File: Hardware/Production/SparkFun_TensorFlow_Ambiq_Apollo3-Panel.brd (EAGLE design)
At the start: 175.6 x 134.7 mm, 906 parts, among them J12 CORTEX_DEBUG, J14 CAMERA-OV7670, J18 CORTEX_DEBUG, J20 CAMERA-OV7670, J24 CORTEX_DEBUG, J26 CAMERA-OV7670, J30 CORTEX_DEBUG, J32 CAMERA-OV7670, J36 CORTEX_DEBUG, J38 CAMERA-OV7670, J42 CORTEX_DEBUG, J44 CAMERA-OV7670, J48 CORTEX_DEBUG, J5 CORTEX_DEBUG, J50 CAMERA-OV7670, J54 CORTEX_DEBUG, J6 CAMERA-OV7670, J8 CAMERA-OV7670, U1 LIS2DH12, U10 LIS2DH12, U11 1.8V, U12 ARTEMIS_MODULESMD, U13 LIS2DH12, U14 1.8V, U15 ARTEMIS_MODULESMD, U16 LIS2DH12, U17 1.8V, U18 ARTEMIS_MODULESMD, U19 LIS2DH12, U2 LIS2DH12, U20 1.8V, U21 ARTEMIS_MODULESMD, U22 LIS2DH12, U23 1.8V, U24 ARTEMIS_MODULESMD, U25 LIS2DH12, U26 1.8V, U27 ARTEMIS_MODULESMD, U3 1.8V, U4 1.8V, U5 ARTEMIS_MODULESMD, U6 ARTEMIS_MODULESMD, U7 LIS2DH12, U8 1.8V, U9 ARTEMIS_MODULESMD, Y1 32.768kHz, Y2 32.768kHz, Y3 32.768kHz, Y4 32.768kHz, Y5 32.768kHz, Y6 32.768kHz, Y7 32.768kHz, Y8 32.768kHz, Y9 32.768kHz

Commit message: Adding panel files for v2.1
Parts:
- removed R127, R128, R129, R130, R138, R139, R145, R146, R147, R148, R156, R157: 4.7k, SparkFun-Resistors:0603
- removed R131, R136, R137, R140, R141, R149, R154, R155, R158, R159: 10k, SparkFun-Resistors:0402-TIGHT
- removed R132, R133, R134, R135, R150, R151, R152, R153: 1k, SparkFun-Resistors:0603
- removed R142, R144, R160, R162: 100k, SparkFun-Resistors:0603
- removed R143, R161: 10k, SparkFun-Resistors:0603
- J10, J16, J22, J28, J34, J40, J46, J52: device SparkFun-Connectors:1X05_NO_SILK -> SparkFun-Connectors:JST04_1MM_RA
- J11, J17, J23, J29, J35, J41, J47, J53: value (none) -> CORTEX_DEBUG; device SparkFun-Connectors:JST04_1MM_RA -> SparkFun-Connectors:2X5-PTH-1.27MM
- J12, J18, J24, J30, J36, J42, J48, J54: value CORTEX_DEBUG -> CAMERA-HIMAX; device SparkFun-Connectors:2X5-PTH-1.27MM -> SparkFun-Connectors:FPC-24-AMPHENOL-SFV24R-1STE1HLF
- J14, J20, J26, J32, J38, J44, J50, J8: value CAMERA-OV7670 -> (none); device SparkFun-Connectors:FPC-24-AMPHENOL-SFV24R-1STE1HLF -> SparkFun-Connectors:1X05_NO_SILK
- J6: value CAMERA-OV7670 -> (none); device SparkFun-Connectors:FPC-24-AMPHENOL-SFV24R-1STE1HLF -> SparkFun-Connectors:1X06-SMD_RA_MALE
- J7: value (none) -> CAMERA-HIMAX; device SparkFun-Connectors:1X06-SMD_RA_MALE -> SparkFun-Connectors:FPC-24-AMPHENOL-SFV24R-1STE1HLF
- R10, R104, R105, R118, R119, R33, R47, R50, R64, R77, R9: value 10k -> 1k; device SparkFun-Resistors:0402-TIGHT -> SparkFun-Resistors:0603
- R100, R101, R113, R32, R46, R59, R86, R87: value 10k -> 4.7k; device SparkFun-Resistors:0402-TIGHT -> SparkFun-Resistors:0603
- R103, R120, R48, R49, R75, R76, R91, R92: value 4.7k -> 1k
- R106, R34, R36, R90: value 100k -> 1k
- R107, R53: device SparkFun-Resistors:0603 -> SparkFun-Resistors:0402-TIGHT
- R108, R52: value 100k -> 10k; device SparkFun-Resistors:0603 -> SparkFun-Resistors:0402-TIGHT
- R109, R121, R37, R38, R39, R66, R67, R93, R94: value 4.7k -> 10k; device SparkFun-Resistors:0603 -> SparkFun-Resistors:0402-TIGHT
- R110, R112, R23, R40, R56, R84: value 4.7k -> 100k
- R111, R55: value 4.7k -> 10k
- R114, R115, R116, R43, R44, R45, R60, R99: value 1k -> 4.7k
- R18, R19, R79, R80, R81: value 1k -> 10k; device SparkFun-Resistors:0603 -> SparkFun-Resistors:0402-TIGHT
- R21, R68, R82: value 10k -> 100k; device SparkFun-Resistors:0402-TIGHT -> SparkFun-Resistors:0603
- R22, R41, R69, R83: device SparkFun-Resistors:0402-TIGHT -> SparkFun-Resistors:0603
- R35, R89: value 10k -> 1k
- R42, R96, R98: value 1k -> 100k
- R71: value 10k -> 4.7k
- R72, R88: value 100k -> 4.7k
- R97: value 1k -> 10k
- S1, S2, S3, S4, S5, S6, S7, S8, S9: device SparkFun-Switches:TACTILE_SWITCH_SMD_5.2MM -> SparkFun-Switches:TACTILE_SWITCH_SMD_4.6X2.8MM
- U12, U15, U18, U21, U24, U27, U5, U6, U9: device Testing:ARTEMIS_FP -> SparkFun-IC-Microcontroller:ARTEMIS_FP
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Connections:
- removed net CAMERA_HREF: J6.9, U5.~AD13
- removed net CAMERA_HREF1: J8.9, U6.~AD13
- removed net CAMERA_HREF2: J14.9, U9.~AD13
- removed net CAMERA_HREF3: J20.9, U12.~AD13
- removed net CAMERA_HREF4: J26.9, U15.~AD13
- removed net CAMERA_HREF5: J32.9, U18.~AD13
- removed net CAMERA_HREF6: J38.9, U21.~AD13
- removed net CAMERA_HREF7: J44.9, U24.~AD13
- removed net CAMERA_HREF8: J50.9, U27.~AD13
- removed net CAMERA_PWDN: J6.8, R22.2, U5.D15
- removed net CAMERA_PWDN1: J8.8, R21.2, U6.D15
- removed net CAMERA_PWDN2: J14.8, R47.2, U9.D15
- removed net CAMERA_PWDN3: J20.8, R65.2, U12.D15
- removed net CAMERA_PWDN4: J26.8, R83.2, U15.D15
- removed net CAMERA_PWDN5: J32.8, R101.2, U18.D15
- removed net CAMERA_PWDN6: J38.8, R119.2, U21.D15
- removed net CAMERA_PWDN7: J44.8, R137.2, U24.D15
- removed net CAMERA_PWDN8: J50.8, R155.2, U27.D15
- removed net CAMERA_RESET: J6.6, R10.1, U5.~AD11
- removed net CAMERA_RESET1: J8.6, R9.1, U6.~AD11
- removed net CAMERA_RESET2: J14.6, R41.1, U9.~AD11
- removed net CAMERA_RESET3: J20.6, R59.1, U12.~AD11
- removed net CAMERA_RESET4: J26.6, R77.1, U15.~AD11
- removed net CAMERA_RESET5: J32.6, R95.1, U18.~AD11
- removed net CAMERA_RESET6: J38.6, R113.1, U21.~AD11
- removed net CAMERA_RESET7: J44.6, R131.1, U24.~AD11
- removed net CAMERA_RESET8: J50.6, R149.1, U27.~AD11
- removed net CAMERA_XCLK: J6.13, U5.~AD32
- removed net CAMERA_XCLK1: J8.13, U6.~AD32
- removed net CAMERA_XCLK2: J14.13, U9.~AD32
- removed net CAMERA_XCLK3: J20.13, U12.~AD32
- removed net CAMERA_XCLK4: J26.13, U15.~AD32
- removed net CAMERA_XCLK5: J32.13, U18.~AD32
- removed net CAMERA_XCLK6: J38.13, U21.~AD32
- removed net CAMERA_XCLK7: J44.13, U24.~AD32
- removed net CAMERA_XCLK8: J50.13, U27.~AD32
- removed net CAMERA_Y0: J6.19, U5.~D22
- removed net CAMERA_Y1: J6.21, U5.~D4
- removed net CAMERA_Y10: J8.22, U6.~AD35
- removed net CAMERA_Y11: J8.18, U6.~D23
- removed net CAMERA_Y12: J8.19, U6.~D22
- removed net CAMERA_Y13: J8.12, U6.~D26
- removed net CAMERA_Y14: J8.14, U6.~D6
- removed net CAMERA_Y15: J8.16, U6.~D28
- removed net CAMERA_Y16: J14.20, U9.~D24
- removed net CAMERA_Y17: J14.21, U9.~D4
- removed net CAMERA_Y18: J14.22, U9.~AD35
- removed net CAMERA_Y19: J14.18, U9.~D23
- removed net CAMERA_Y2: J6.22, U5.~AD35
- removed net CAMERA_Y20: J14.19, U9.~D22
- removed net CAMERA_Y21: J14.12, U9.~D26
- removed net CAMERA_Y22: J14.14, U9.~D6
- removed net CAMERA_Y23: J14.16, U9.~D28
- removed net CAMERA_Y24: J20.20, U12.~D24
- removed net CAMERA_Y25: J20.21, U12.~D4
- removed net CAMERA_Y26: J20.22, U12.~AD35
- removed net CAMERA_Y27: J20.18, U12.~D23
- removed net CAMERA_Y28: J20.19, U12.~D22
- removed net CAMERA_Y29: J20.12, U12.~D26
- removed net CAMERA_Y3: J6.20, U5.~D24
- removed net CAMERA_Y30: J20.14, U12.~D6
- removed net CAMERA_Y31: J20.16, U12.~D28
- removed net CAMERA_Y32: J26.20, U15.~D24
- removed net CAMERA_Y33: J26.21, U15.~D4
- removed net CAMERA_Y34: J26.22, U15.~AD35
- removed net CAMERA_Y35: J26.18, U15.~D23
- removed net CAMERA_Y36: J26.19, U15.~D22
- removed net CAMERA_Y37: J26.12, U15.~D26
- removed net CAMERA_Y38: J26.14, U15.~D6
- removed net CAMERA_Y39: J26.16, U15.~D28
- removed net CAMERA_Y4: J6.18, U5.~D23
- removed net CAMERA_Y40: J32.20, U18.~D24
- removed net CAMERA_Y41: J32.21, U18.~D4
- removed net CAMERA_Y42: J32.22, U18.~AD35
- removed net CAMERA_Y43: J32.18, U18.~D23
- removed net CAMERA_Y44: J32.19, U18.~D22
- removed net CAMERA_Y45: J32.12, U18.~D26
- removed net CAMERA_Y46: J32.14, U18.~D6
- removed net CAMERA_Y47: J32.16, U18.~D28
- removed net CAMERA_Y48: J38.20, U21.~D24
- removed net CAMERA_Y49: J38.21, U21.~D4
- removed net CAMERA_Y5: J6.16, U5.~D28
- removed net CAMERA_Y50: J38.22, U21.~AD35
- removed net CAMERA_Y51: J38.18, U21.~D23
- removed net CAMERA_Y52: J38.19, U21.~D22
- removed net CAMERA_Y53: J38.12, U21.~D26
- removed net CAMERA_Y54: J38.14, U21.~D6
- removed net CAMERA_Y55: J38.16, U21.~D28
- removed net CAMERA_Y56: J44.20, U24.~D24
- removed net CAMERA_Y57: J44.21, U24.~D4
- removed net CAMERA_Y58: J44.22, U24.~AD35
- removed net CAMERA_Y59: J44.18, U24.~D23
- removed net CAMERA_Y6: J6.14, U5.~D6
- removed net CAMERA_Y60: J44.19, U24.~D22
- removed net CAMERA_Y61: J44.12, U24.~D26
- removed net CAMERA_Y62: J44.14, U24.~D6
- removed net CAMERA_Y63: J44.16, U24.~D28
- removed net CAMERA_Y64: J50.20, U27.~D24
- removed net CAMERA_Y65: J50.21, U27.~D4
- removed net CAMERA_Y66: J50.22, U27.~AD35
- removed net CAMERA_Y67: J50.18, U27.~D23
- removed net CAMERA_Y68: J50.19, U27.~D22
- removed net CAMERA_Y69: J50.12, U27.~D26
- removed net CAMERA_Y7: J6.12, U5.~D26
- removed net CAMERA_Y70: J50.14, U27.~D6
- removed net CAMERA_Y71: J50.16, U27.~D28
- removed net CAMERA_Y8: J8.20, U6.~D24
- removed net CAMERA_Y9: J8.21, U6.~D4
- new net CAMERA_D0: J7.14, U5.D14
- new net CAMERA_D1: J7.3, U5.~AD11
- new net CAMERA_D10: J12.9, U6.~D25
- new net CAMERA_D11: J12.12, U6.~D6
- new net CAMERA_D12: J12.14, U6.D14
- new net CAMERA_D13: J12.13, U6.~D28
- new net CAMERA_D14: J12.19, U6.~AD35
- new net CAMERA_D15: J12.20, U6.~D5
- new net CAMERA_D16: J18.5, U9.AD34
- new net CAMERA_D17: J18.3, U9.~AD11
- new net CAMERA_D18: J18.9, U9.~D25
- new net CAMERA_D19: J18.12, U9.~D6
- new net CAMERA_D2: J7.9, U5.~D25
- new net CAMERA_D20: J18.14, U9.D14
- new net CAMERA_D21: J18.13, U9.~D28
- new net CAMERA_D22: J18.19, U9.~AD35
- new net CAMERA_D23: J18.20, U9.~D5
- new net CAMERA_D24: J24.5, U12.AD34
- new net CAMERA_D25: J24.3, U12.~AD11
- new net CAMERA_D26: J24.9, U12.~D25
- new net CAMERA_D27: J24.12, U12.~D6
- new net CAMERA_D28: J24.14, U12.D14
- new net CAMERA_D29: J24.13, U12.~D28
- new net CAMERA_D3: J7.5, U5.AD34
- new net CAMERA_D30: J24.19, U12.~AD35
- new net CAMERA_D31: J24.20, U12.~D5
- new net CAMERA_D32: J30.5, U15.AD34
- new net CAMERA_D33: J30.3, U15.~AD11
- new net CAMERA_D34: J30.9, U15.~D25
- new net CAMERA_D35: J30.12, U15.~D6
- new net CAMERA_D36: J30.14, U15.D14
- new net CAMERA_D37: J30.13, U15.~D28
- new net CAMERA_D38: J30.19, U15.~AD35
- new net CAMERA_D39: J30.20, U15.~D5
- new net CAMERA_D4: J7.12, U5.~D6
- new net CAMERA_D40: J36.5, U18.AD34
- new net CAMERA_D41: J36.3, U18.~AD11
- new net CAMERA_D42: J36.9, U18.~D25
- new net CAMERA_D43: J36.12, U18.~D6
- new net CAMERA_D44: J36.14, U18.D14
- new net CAMERA_D45: J36.13, U18.~D28
- new net CAMERA_D46: J36.19, U18.~AD35
- new net CAMERA_D47: J36.20, U18.~D5
- new net CAMERA_D48: J42.5, U21.AD34
- new net CAMERA_D49: J42.3, U21.~AD11
- new net CAMERA_D5: J7.20, U5.~D5
- new net CAMERA_D50: J42.9, U21.~D25
- new net CAMERA_D51: J42.12, U21.~D6
- new net CAMERA_D52: J42.14, U21.D14
- new net CAMERA_D53: J42.13, U21.~D28
- new net CAMERA_D54: J42.19, U21.~AD35
- new net CAMERA_D55: J42.20, U21.~D5
- new net CAMERA_D56: J48.5, U24.AD34
- new net CAMERA_D57: J48.3, U24.~AD11
- new net CAMERA_D58: J48.9, U24.~D25
- new net CAMERA_D59: J48.12, U24.~D6
- new net CAMERA_D6: J7.19, U5.~AD35
- new net CAMERA_D60: J48.14, U24.D14
- new net CAMERA_D61: J48.13, U24.~D28
- new net CAMERA_D62: J48.19, U24.~AD35
- new net CAMERA_D63: J48.20, U24.~D5
- new net CAMERA_D64: J54.5, U27.AD34
- new net CAMERA_D65: J54.3, U27.~AD11
- new net CAMERA_D66: J54.9, U27.~D25
- new net CAMERA_D67: J54.12, U27.~D6
- new net CAMERA_D68: J54.14, U27.D14
- new net CAMERA_D69: J54.13, U27.~D28
- new net CAMERA_D7: J7.13, U5.~D28
- new net CAMERA_D70: J54.19, U27.~AD35
- new net CAMERA_D71: J54.20, U27.~D5
- new net CAMERA_D8: J12.5, U6.AD34
- new net CAMERA_D9: J12.3, U6.~AD11
- new net CAMERA_HSYNC: J7.16, U5.~D27
- new net CAMERA_HSYNC1: J12.16, U6.~D27
- new net CAMERA_HSYNC2: J18.16, U9.~D27
- new net CAMERA_HSYNC3: J24.16, U12.~D27
- new net CAMERA_HSYNC4: J30.16, U15.~D27
- new net CAMERA_HSYNC5: J36.16, U18.~D27
- new net CAMERA_HSYNC6: J42.16, U21.~D27
- new net CAMERA_HSYNC7: J48.16, U24.~D27
- new net CAMERA_HSYNC8: J54.16, U27.~D27
- new net CAMERA_INT: J7.18, U5.~D23
- new net CAMERA_INT1: J12.18, U6.~D23
- new net CAMERA_INT2: J18.18, U9.~D23
- new net CAMERA_INT3: J24.18, U12.~D23
- new net CAMERA_INT4: J30.18, U15.~D23
- new net CAMERA_INT5: J36.18, U18.~D23
- new net CAMERA_INT6: J42.18, U21.~D23
- new net CAMERA_INT7: J48.18, U24.~D23
- new net CAMERA_INT8: J54.18, U27.~D23
- new net CAMERA_MCLK: J7.8, U5.~D26
- new net CAMERA_MCLK1: J12.8, U6.~D26
- new net CAMERA_MCLK2: J18.8, U9.~D26
- new net CAMERA_MCLK3: J24.8, U12.~D26
- new net CAMERA_MCLK4: J30.8, U15.~D26
- new net CAMERA_MCLK5: J36.8, U18.~D26
- new net CAMERA_MCLK6: J42.8, U21.~D26
- new net CAMERA_MCLK7: J48.8, U24.~D26
- new net CAMERA_MCLK8: J54.8, U27.~D26
- new net CAMERA_TRIG: J7.7, U5.~AD13
- new net CAMERA_TRIG1: J12.7, U6.~AD13
- new net CAMERA_TRIG2: J18.7, U9.~AD13
- new net CAMERA_TRIG3: J24.7, U12.~AD13
- new net CAMERA_TRIG4: J30.7, U15.~AD13
- new net CAMERA_TRIG5: J36.7, U18.~AD13
- new net CAMERA_TRIG6: J42.7, U21.~AD13
- new net CAMERA_TRIG7: J48.7, U24.~AD13
- new net CAMERA_TRIG8: J54.7, U27.~AD13
- net !DTR1: now also J6.1, R23.2; no longer J7.1, R36.2
- net !DTR2: now also R42.2; no longer R54.2
- net !DTR3: now also R56.2; no longer R72.2
- net !DTR4: now also R70.2; no longer R90.2
- net !DTR5: now also R84.2; no longer R108.2
- net !DTR6: now also R98.2; no longer R126.2
- net !DTR7: now also R112.2; no longer R144.2
- net !DTR8: now also R126.2; no longer R162.2
- net 1.8V: now also J7.10; no longer J6.10
- net 1.8V1: now also J12.10; no longer J8.10
- net 1.8V2: now also J18.10; no longer J14.10
- net 1.8V3: now also J24.10; no longer J20.10
- net 1.8V4: now also J30.10; no longer J26.10
- net 1.8V5: now also J36.10; no longer J32.10
- net 1.8V6: now also J42.10; no longer J38.10
- net 1.8V7: now also J48.10; no longer J44.10
- net 1.8V8: now also J54.10; no longer J50.10
- net A1: now also J8.2; no longer J9.2
- net A2: now also J14.2; no longer J15.2
- net A3: now also J20.2; no longer J21.2
- net A4: now also J26.2; no longer J27.2
- net A5: now also J32.2; no longer J33.2
- net A6: now also J38.2; no longer J39.2
- net A7: now also J44.2; no longer J45.2
- net A8: now also J50.2; no longer J51.2
- net ACCEL_I2C_SCL2: now also R31.1; no longer R39.1
- net ACCEL_I2C_SCL3: now also R45.1; no longer R57.1
- net ACCEL_I2C_SCL4: now also R59.1; no longer R75.1
- net ACCEL_I2C_SCL5: now also R73.1; no longer R93.1
- net ACCEL_I2C_SCL6: now also R87.1; no longer R111.1
- net ACCEL_I2C_SCL7: now also R101.1; no longer R129.1
- net ACCEL_I2C_SCL8: now also R115.1; no longer R147.1
- net ACCEL_I2C_SDA2: now also R32.1; no longer R40.1
- net ACCEL_I2C_SDA3: now also R46.1; no longer R58.1
- net ACCEL_I2C_SDA4: now also R60.1; no longer R76.1
- net ACCEL_I2C_SDA5: now also R74.1; no longer R94.1
- net ACCEL_I2C_SDA6: now also R88.1; no longer R112.1
- net ACCEL_I2C_SDA7: now also R102.1; no longer R130.1
- net ACCEL_I2C_SDA8: now also R116.1; no longer R148.1
- net ACCEL_INT10: now also R66.2; no longer R86.2
- net ACCEL_INT11: now also R81.2; no longer R105.2
- net ACCEL_INT12: now also R80.2; no longer R104.2
- net ACCEL_INT13: now also R95.2; no longer R123.2
- net ACCEL_INT14: now also R94.2; no longer R122.2
- net ACCEL_INT15: now also R109.2; no longer R141.2
- net ACCEL_INT16: now also R108.2; no longer R140.2
- net ACCEL_INT17: now also R123.2; no longer R159.2
- net ACCEL_INT18: now also R122.2; no longer R158.2
- net ACCEL_INT3: now also R20.2; no longer R33.2
- net ACCEL_INT4: now also R19.2; no longer R32.2
- net ACCEL_INT5: now also R39.2; no longer R51.2
- net ACCEL_INT6: now also R38.2; no longer R50.2
- net ACCEL_INT7: now also R53.2; no longer R69.2
- net ACCEL_INT8: now also R52.2; no longer R68.2
- net ACCEL_INT9: now also R67.2; no longer R87.2
- net AMBIQ_!RST: now also S3.4
- net AMBIQ_!RST1: now also J11.10, R21.1, S1.4; no longer J12.10, R34.1
- net AMBIQ_!RST2: now also J17.10, R40.1, S2.4; no longer J18.10, R52.1
- net AMBIQ_!RST3: now also J23.10, R54.1, S4.4; no longer J24.10, R70.1
- net AMBIQ_!RST4: now also J29.10, R68.1, S5.4; no longer J30.10, R88.1
- net AMBIQ_!RST5: now also J35.10, R82.1, S6.4; no longer J36.10, R106.1
- net AMBIQ_!RST6: now also J41.10, R96.1, S7.4; no longer J42.10, R124.1
- net AMBIQ_!RST7: now also J47.10, R110.1, S8.4; no longer J48.10, R142.1
- net AMBIQ_!RST8: now also J53.10, R124.1, S9.4; no longer J54.10, R160.1
- net BOOT1: now also R22.2; no longer R35.2
- net BOOT2: now also R41.2; no longer R53.2
- net BOOT3: now also R55.2; no longer R71.2
- net BOOT4: now also R69.2; no longer R89.2
- net BOOT5: now also R83.2; no longer R107.2
- net BOOT6: now also R97.2; no longer R125.2
- net BOOT7: now also R111.2; no longer R143.2
- net BOOT8: now also R125.2; no longer R161.2
- net CAMERA_DVDD_EN: now also U5.~AD32; no longer U5.D7
- net CAMERA_DVDD_EN1: now also R18.2, U6.~AD32; no longer R20.2, U6.D7
- net CAMERA_DVDD_EN2: now also R37.2, U9.~AD32; no longer R46.2, U9.D7
- net CAMERA_DVDD_EN3: now also R51.2, U12.~AD32; no longer R64.2, U12.D7
- net CAMERA_DVDD_EN4: now also R65.2, U15.~AD32; no longer R82.2, U15.D7
- net CAMERA_DVDD_EN5: now also R79.2, U18.~AD32; no longer R100.2, U18.D7
- net CAMERA_DVDD_EN6: now also R93.2, U21.~AD32; no longer R118.2, U21.D7
- net CAMERA_DVDD_EN7: now also R107.2, U24.~AD32; no longer R136.2, U24.D7
- net CAMERA_DVDD_EN8: now also R121.2, U27.~AD32; no longer R154.2, U27.D7
- net CAMERA_I2C_SCL: now also J7.21, U5.D8; no longer J6.5, U5.~D27
- net CAMERA_I2C_SCL1: now also J12.21, U6.D8; no longer J8.5, U6.~D27
- net CAMERA_I2C_SCL2: now also J18.21, R24.1, U9.D8; no longer J14.5, R37.1, U9.~D27
- net CAMERA_I2C_SCL3: now also J24.21, R43.1, U12.D8; no longer J20.5, R55.1, U12.~D27
- net CAMERA_I2C_SCL4: now also J30.21, R57.1, U15.D8; no longer J26.5, R73.1, U15.~D27
- net CAMERA_I2C_SCL5: now also J36.21, R71.1, U18.D8; no longer J32.5, R91.1, U18.~D27
- net CAMERA_I2C_SCL6: now also J42.21, R85.1, U21.D8; no longer J38.5, R109.1, U21.~D27
- net CAMERA_I2C_SCL7: now also J48.21, R99.1, U24.D8; no longer J44.5, R127.1, U24.~D27
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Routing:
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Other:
- board size 175.6 x 134.7 mm -> 177.7 x 134.7 mm
- board text added: "v21"
- board text removed: "v20"

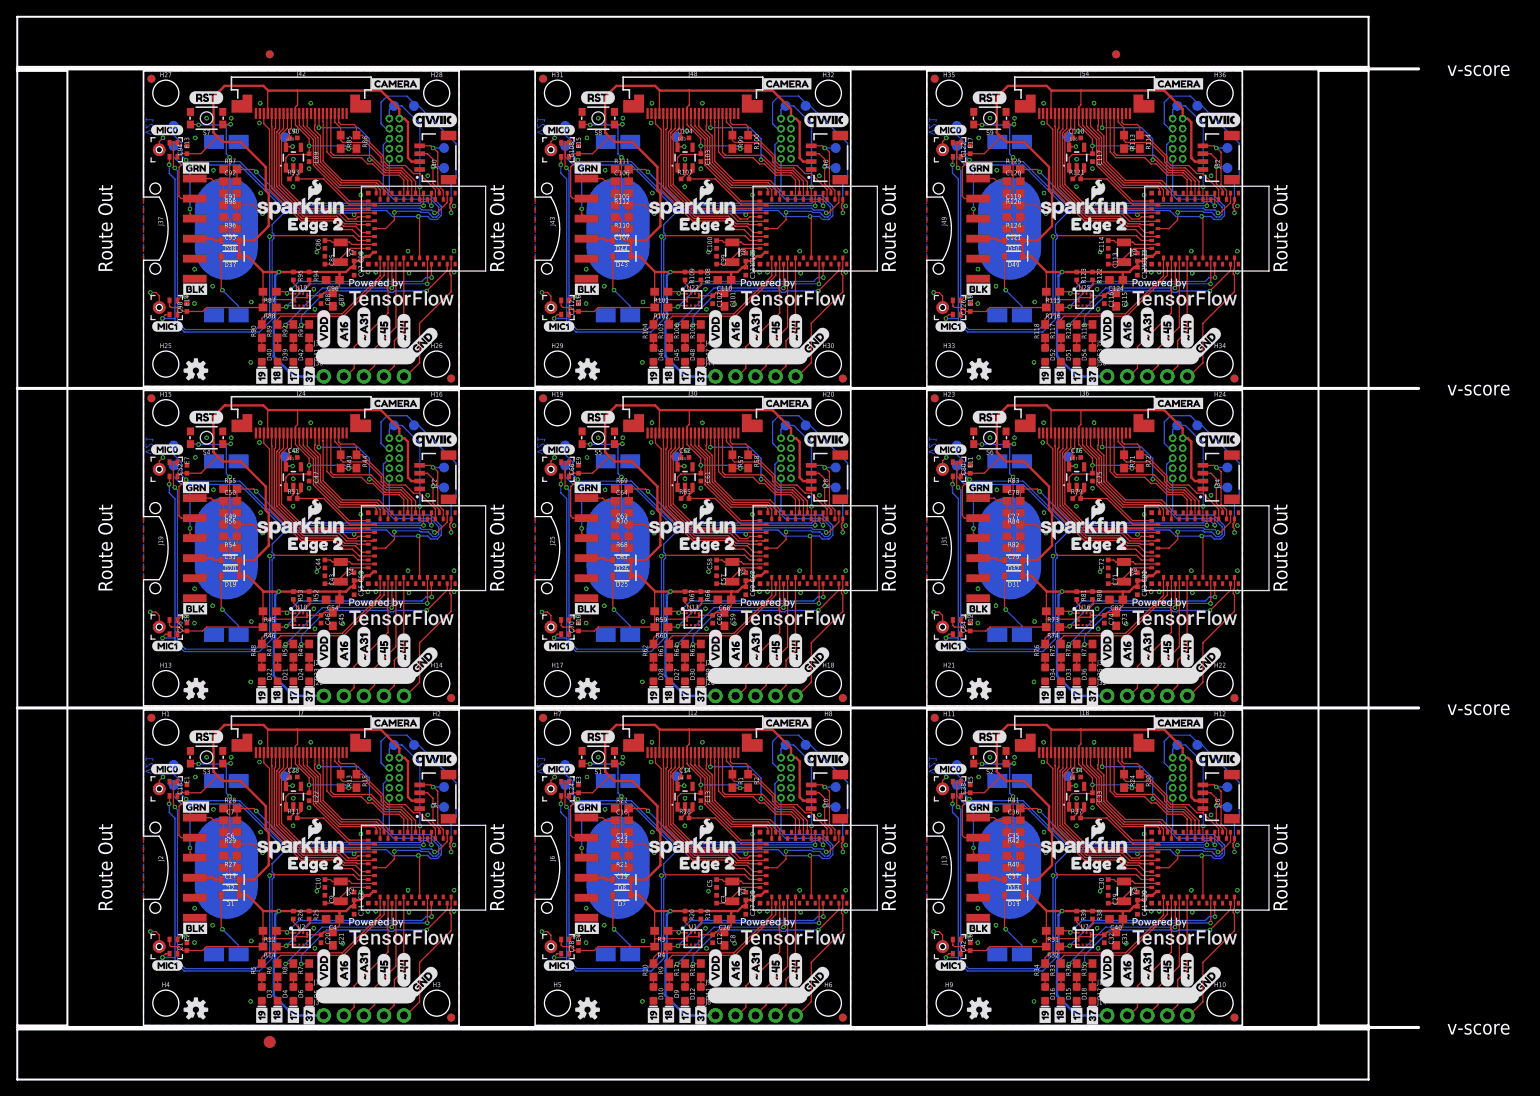
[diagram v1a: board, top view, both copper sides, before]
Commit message: Add power control via GPIO to accel and mics.
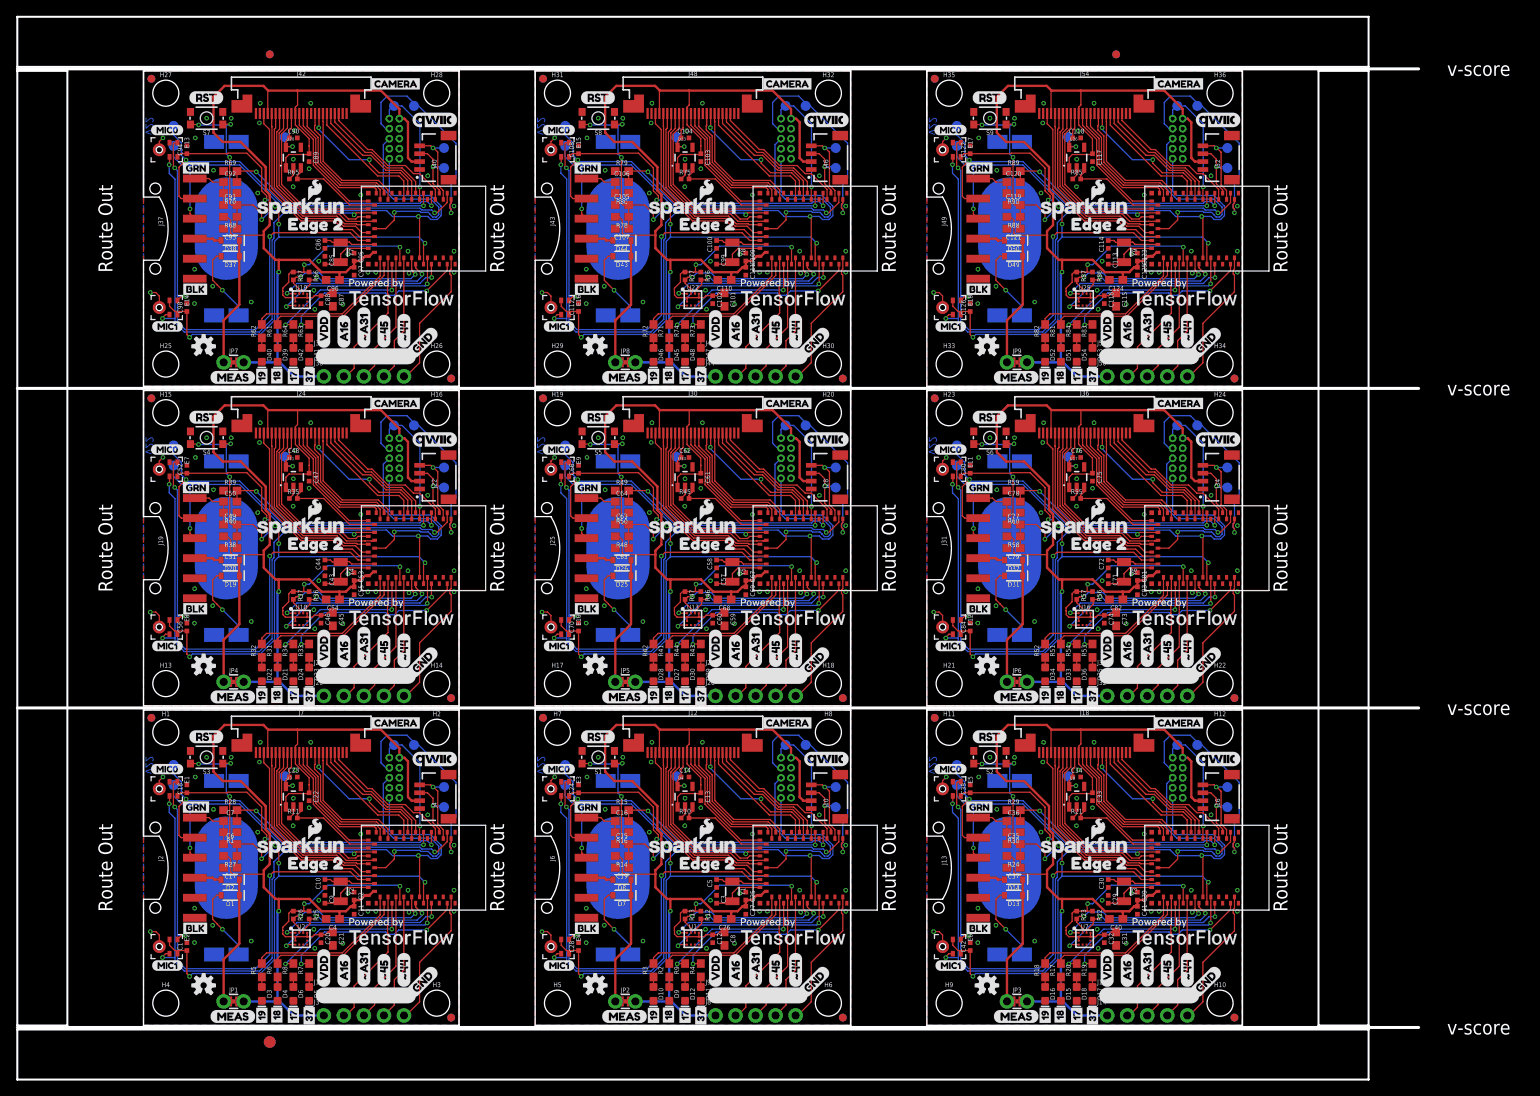
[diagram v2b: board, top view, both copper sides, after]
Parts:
- removed R100, R101, R102, R113, R114, R115, R116, R99: 4.7k, SparkFun-Resistors:0603
- removed R103, R104, R105, R106, R117, R118, R119, R120, R91, R92: 1k, SparkFun-Resistors:0603
- removed R107, R108, R109, R121, R122, R123, R93, R94, R95: 10k, SparkFun-Resistors:0402-TIGHT
- removed R110, R112, R124, R126, R96, R98: 100k, SparkFun-Resistors:0603
- removed R111, R125, R97: 10k, SparkFun-Resistors:0603
- added JP1, JP2, JP3, JP4, JP5, JP6, JP7, JP8, JP9: JUMPER-COMBO_2_NC_TRACE, SparkFun-Jumpers:COMBO-JUMPER_2_NC_TRACE
- added U$262: (no value), SparkFun-Aesthetics:SFE_LOGO_NAME_.1
- added U$263: (no value), SparkFun-Aesthetics:OSHW-LOGO-S
- added U$264, U$272: (no value), buzzard_labels (9):#444
- added U$265, U$271: (no value), buzzard_labels (9):#453
- added U$266, U$270: (no value), buzzard_labels (9):#A312
- added U$267, U$269: (no value), buzzard_labels (9):A161
- added U$268: (no value), buzzard_labels (9):MIC10
- added U$273, U$277: (no value), buzzard_labels (11):EDGE_20
- added U$274: (no value), buzzard_labels (13):171
- added U$275: (no value), buzzard_labels (14):182
- added U$276: (no value), buzzard_labels (14):193
- added U$278, U$279: (no value), buzzard_labels (1):MEAS10
- C106, C120, C16, C36, C50, C64, C7, C78, C92: value 2.2uF -> 0.1uF
- R1, R14, R24, R30, R58, R60, R88: value 4.7k -> 100k
- R10, R35, R36, R47, R75, R76, R77: value 1k -> 100k; device SparkFun-Resistors:0603 -> SparkFun-Resistors:0402-TIGHT
- R11, R25, R26, R37, R65, R66, R67: value 10k -> 100k
- R12, R13, R45, R46, R57, R85, R86, R87: value 4.7k -> 100k; device SparkFun-Resistors:0603 -> SparkFun-Resistors:0402-TIGHT
- R15, R59: value 4.7k -> 220k
- R16, R48, R50, R78, R90: value 1k -> 100k
- R18, R19, R20, R51, R52, R53, R81: value 10k -> 1k; device SparkFun-Resistors:0402-TIGHT -> SparkFun-Resistors:0603
- R2, R3, R31, R32, R4, R43, R44, R71, R72, R73, R74: value 4.7k -> 1k
- R21, R23, R56: device SparkFun-Resistors:0603 -> SparkFun-Resistors:0402-TIGHT
- R22, R55: value 10k -> 100k; device SparkFun-Resistors:0603 -> SparkFun-Resistors:0402-TIGHT
- R28, R69: value 10k -> 220k
- R29: value 100k -> 220k
- R38, R80: value 10k -> 100k; device SparkFun-Resistors:0402-TIGHT -> SparkFun-Resistors:0603
- R39, R79: value 10k -> 220k; device SparkFun-Resistors:0402-TIGHT -> SparkFun-Resistors:0603
- R41, R83: value 10k -> 1k
- R42, R54, R82, R84: value 100k -> 1k
- R49, R89: value 1k -> 220k
- U$100, U$69: device PoweredBy_TF#jpg:POWEREDBY_TF#JPG -> buzzard_labels:GRN1
- U$101: device SparkFun-Aesthetics:SFE_LOGO_NAME_.1 -> buzzard_labels:372
- U$102: device SparkFun-Aesthetics:OSHW-LOGO-S -> Labels:QWIIC_COPYRIGHT_SMALL
- U$103, U$227: device buzzard_labels (9):#444 -> buzzard_labels:CAMERA3
- U$104, U$168, U$197, U$75: device buzzard_labels (9):#453 -> PoweredBy_TF#jpg:POWEREDBY_TF#JPG
- U$105, U$167: device buzzard_labels (9):#A312 -> buzzard_labels:MIC00
- U$106, U$135, U$137, U$166: device buzzard_labels (9):A161 -> PoweredBy_TF#jpg:POWEREDBY_TF#JPG
- U$107: device buzzard_labels (9):MIC10 -> SparkFun-Aesthetics:SFE_LOGO_NAME_.1
- U$108, U$77: device buzzard_labels (9):A161 -> SparkFun-Aesthetics:OSHW-LOGO-S
- U$109, U$47: device buzzard_labels (9):#A312 -> buzzard_labels (9):#444
- U$111, U$53: device buzzard_labels (9):#444 -> buzzard_labels (9):#A312
- U$112, U$145, U$174, U$83: device buzzard_labels (11):EDGE_20 -> buzzard_labels (9):A161
- U$113: device buzzard_labels (13):171 -> buzzard_labels (9):MIC10
- U$114, U$143: device buzzard_labels (14):182 -> buzzard_labels (9):A161
- U$115, U$173: device buzzard_labels (14):193 -> buzzard_labels (9):#A312
- U$116, U$141, U$203, U$54: device buzzard_labels (11):EDGE_20 -> buzzard_labels (9):#453
- U$117, U$233: device buzzard_labels:GND0 -> buzzard_labels (9):#444
- U$118, U$60: device buzzard_labels:VDD1 -> buzzard_labels (11):EDGE_20
- U$119: device buzzard_labels:VDD1 -> buzzard_labels (13):171
- U$120: device buzzard_labels:GND0 -> buzzard_labels (14):182
- U$121: device buzzard_labels:RST15 -> buzzard_labels (14):193
- U$122, U$180: device buzzard_labels:BLK2 -> buzzard_labels (11):EDGE_20
- U$123, U$35: device buzzard_labels:GRN1 -> buzzard_labels (1):MEAS10
- U$124: device buzzard_labels:372 -> buzzard_labels (1):MEAS10
- U$125: device Labels:QWIIC_COPYRIGHT_SMALL -> buzzard_labels:GND0
- U$126: device buzzard_labels:CAMERA3 -> buzzard_labels:VDD1
- U$127, U$158: device PoweredBy_TF#jpg:POWEREDBY_TF#JPG -> buzzard_labels:VDD1
- U$128: device buzzard_labels:MIC00 -> buzzard_labels:GND0
- U$129, U$98: device PoweredBy_TF#jpg:POWEREDBY_TF#JPG -> buzzard_labels:RST15
- U$130: device SparkFun-Aesthetics:SFE_LOGO_NAME_.1 -> buzzard_labels:BLK2
- U$131: device SparkFun-Aesthetics:OSHW-LOGO-S -> buzzard_labels:GRN1
- U$132, U$256: device buzzard_labels (9):#444 -> buzzard_labels:372
- U$133, U$226: device buzzard_labels (9):#453 -> Labels:QWIIC_COPYRIGHT_SMALL
- U$134, U$196: device buzzard_labels (9):#A312 -> buzzard_labels:CAMERA3
- U$136: device buzzard_labels (9):MIC10 -> buzzard_labels:MIC00
- U$138, U$76: device buzzard_labels (9):#A312 -> SparkFun-Aesthetics:SFE_LOGO_NAME_.1
- U$139, U$46: device buzzard_labels (9):#453 -> SparkFun-Aesthetics:OSHW-LOGO-S
- U$142, U$84: device buzzard_labels (13):171 -> buzzard_labels (9):#A312
- U$144: device buzzard_labels (14):193 -> buzzard_labels (9):MIC10
- U$146, U$204: device buzzard_labels:GND0 -> buzzard_labels (9):#A312
- U$147, U$234: device buzzard_labels:VDD1 -> buzzard_labels (9):#453
- U$148: device buzzard_labels:VDD1 -> buzzard_labels (9):#444
- U$149, U$91: device buzzard_labels:GND0 -> buzzard_labels (11):EDGE_20
- U$150: device buzzard_labels:RST15 -> buzzard_labels (13):171
- U$151: device buzzard_labels:BLK2 -> buzzard_labels (14):182
- U$152: device buzzard_labels:GRN1 -> buzzard_labels (14):193
- U$153, U$211: device buzzard_labels:372 -> buzzard_labels (11):EDGE_20
- U$154: device Labels:QWIIC_COPYRIGHT_SMALL -> buzzard_labels (1):MEAS10
- U$155: device buzzard_labels:CAMERA3 -> buzzard_labels (1):MEAS10
- U$156, U$187: device PoweredBy_TF#jpg:POWEREDBY_TF#JPG -> buzzard_labels:GND0
- U$157: device buzzard_labels:MIC00 -> buzzard_labels:VDD1
- U$159: device SparkFun-Aesthetics:SFE_LOGO_NAME_.1 -> buzzard_labels:GND0
- U$160: device SparkFun-Aesthetics:OSHW-LOGO-S -> buzzard_labels:RST15
- U$161: device buzzard_labels (9):#444 -> buzzard_labels:BLK2
- U$162, U$255: device buzzard_labels (9):#453 -> buzzard_labels:GRN1
- U$163, U$225: device buzzard_labels (9):#A312 -> buzzard_labels:372
- U$164, U$195: device buzzard_labels (9):A161 -> Labels:QWIIC_COPYRIGHT_SMALL
- U$165: device buzzard_labels (9):MIC10 -> buzzard_labels:CAMERA3
- U$169, U$45: device buzzard_labels (9):#444 -> SparkFun-Aesthetics:SFE_LOGO_NAME_.1
- U$170, U$232: device buzzard_labels (11):EDGE_20 -> SparkFun-Aesthetics:OSHW-LOGO-S
- U$171, U$55: device buzzard_labels (13):171 -> buzzard_labels (9):#444
- U$172, U$85: device buzzard_labels (14):182 -> buzzard_labels (9):#453
- U$175: device buzzard_labels:GND0 -> buzzard_labels (9):MIC10
- U$176, U$205: device buzzard_labels:VDD1 -> buzzard_labels (9):A161
- U$177, U$235: device buzzard_labels:VDD1 -> buzzard_labels (9):#A312
- U$178: device buzzard_labels:GND0 -> buzzard_labels (9):#453
- U$179: device buzzard_labels:RST15 -> buzzard_labels (9):#444
- U$181: device buzzard_labels:GRN1 -> buzzard_labels (13):171
- U$182: device buzzard_labels:372 -> buzzard_labels (14):182
- U$183: device Labels:QWIIC_COPYRIGHT_SMALL -> buzzard_labels (14):193
- U$184, U$242: device buzzard_labels:CAMERA3 -> buzzard_labels (11):EDGE_20
- U$185, U$216: device PoweredBy_TF#jpg:POWEREDBY_TF#JPG -> buzzard_labels (1):MEAS10
- U$186: device buzzard_labels:MIC00 -> buzzard_labels (1):MEAS10
- U$188: device SparkFun-Aesthetics:SFE_LOGO_NAME_.1 -> buzzard_labels:VDD1
- U$189: device SparkFun-Aesthetics:OSHW-LOGO-S -> buzzard_labels:VDD1
- U$190: device buzzard_labels (9):#444 -> buzzard_labels:GND0
- U$191: device buzzard_labels (9):#453 -> buzzard_labels:RST15
- U$192, U$254: device buzzard_labels (9):#A312 -> buzzard_labels:BLK2
- U$193, U$224: device buzzard_labels (9):A161 -> buzzard_labels:GRN1
- U$194: device buzzard_labels (9):MIC10 -> buzzard_labels:372
- U$198, U$74: device buzzard_labels (9):#444 -> buzzard_labels:MIC00
- U$199, U$228, U$261: device buzzard_labels (11):EDGE_20 -> PoweredBy_TF#jpg:POWEREDBY_TF#JPG
- U$200: device buzzard_labels (13):171 -> SparkFun-Aesthetics:SFE_LOGO_NAME_.1
- U$201: device buzzard_labels (14):182 -> SparkFun-Aesthetics:OSHW-LOGO-S
- U$202, U$86: device buzzard_labels (14):193 -> buzzard_labels (9):#444
- U$206: device buzzard_labels:VDD1 -> buzzard_labels (9):MIC10
- U$207, U$236: device buzzard_labels:GND0 -> buzzard_labels (9):A161
- U$208: device buzzard_labels:RST15 -> buzzard_labels (9):#A312
- U$209: device buzzard_labels:BLK2 -> buzzard_labels (9):#453
- U$210: device buzzard_labels:GRN1 -> buzzard_labels (9):#444
- U$212: device Labels:QWIIC_COPYRIGHT_SMALL -> buzzard_labels (13):171
- U$213: device buzzard_labels:CAMERA3 -> buzzard_labels (14):182
- U$214, U$245: device PoweredBy_TF#jpg:POWEREDBY_TF#JPG -> buzzard_labels (14):193
- U$215: device buzzard_labels:MIC00 -> buzzard_labels (11):EDGE_20
- U$217: device SparkFun-Aesthetics:SFE_LOGO_NAME_.1 -> buzzard_labels (1):MEAS10
- U$218: device SparkFun-Aesthetics:OSHW-LOGO-S -> buzzard_labels:GND0
- U$219: device buzzard_labels (9):#444 -> buzzard_labels:VDD1
- U$220: device buzzard_labels (9):#453 -> buzzard_labels:VDD1
- U$221: device buzzard_labels (9):#A312 -> buzzard_labels:GND0
- U$222, U$253: device buzzard_labels (9):A161 -> buzzard_labels:RST15
- U$223: device buzzard_labels (9):MIC10 -> buzzard_labels:BLK2
- U$229: device buzzard_labels (13):171 -> buzzard_labels:MIC00
- U$230, U$259: device buzzard_labels (14):182 -> PoweredBy_TF#jpg:POWEREDBY_TF#JPG
- U$231: device buzzard_labels (14):193 -> SparkFun-Aesthetics:SFE_LOGO_NAME_.1
- U$237: device buzzard_labels:RST15 -> buzzard_labels (9):MIC10
- U$238: device buzzard_labels:BLK2 -> buzzard_labels (9):A161
- U$239: device buzzard_labels:GRN1 -> buzzard_labels (9):#A312
- U$24, U$62: device buzzard_labels:GND0 -> buzzard_labels (1):MEAS10
- U$240: device buzzard_labels:372 -> buzzard_labels (9):#453
- U$241: device Labels:QWIIC_COPYRIGHT_SMALL -> buzzard_labels (9):#444
- U$243: device PoweredBy_TF#jpg:POWEREDBY_TF#JPG -> buzzard_labels (13):171
- U$244: device buzzard_labels:MIC00 -> buzzard_labels (14):182
- U$246: device SparkFun-Aesthetics:SFE_LOGO_NAME_.1 -> buzzard_labels (11):EDGE_20
- U$247: device SparkFun-Aesthetics:OSHW-LOGO-S -> buzzard_labels (1):MEAS10
- U$248: device buzzard_labels (9):#444 -> buzzard_labels (1):MEAS10
- U$249: device buzzard_labels (9):#453 -> buzzard_labels:GND0
- U$250: device buzzard_labels (9):#A312 -> buzzard_labels:VDD1
- U$251: device buzzard_labels (9):A161 -> buzzard_labels:VDD1
- U$252: device buzzard_labels (9):MIC10 -> buzzard_labels:GND0
- U$257: device buzzard_labels (11):EDGE_20 -> Labels:QWIIC_COPYRIGHT_SMALL
- U$258: device buzzard_labels (13):171 -> buzzard_labels:CAMERA3
- U$260: device buzzard_labels (14):193 -> buzzard_labels:MIC00
- U$33, U$63: device buzzard_labels:RST15 -> buzzard_labels:GND0
- U$34: device buzzard_labels:BLK2 -> buzzard_labels:RST15
- U$37: device buzzard_labels:372 -> buzzard_labels:BLK2
- U$38: device Labels:QWIIC_COPYRIGHT_SMALL -> buzzard_labels:GRN1
- U$39: device buzzard_labels:CAMERA3 -> buzzard_labels:372
- U$40, U$71: device PoweredBy_TF#jpg:POWEREDBY_TF#JPG -> Labels:QWIIC_COPYRIGHT_SMALL
- U$41: device buzzard_labels:MIC00 -> buzzard_labels:CAMERA3
- U$43: device SparkFun-Aesthetics:SFE_LOGO_NAME_.1 -> buzzard_labels:MIC00
- U$44, U$73: device SparkFun-Aesthetics:OSHW-LOGO-S -> PoweredBy_TF#jpg:POWEREDBY_TF#JPG
- U$48, U$79: device buzzard_labels (9):A161 -> buzzard_labels (9):#453
- U$49: device buzzard_labels (9):MIC10 -> buzzard_labels (9):#A312
- U$51: device buzzard_labels (9):#A312 -> buzzard_labels (9):MIC10
- U$52, U$81: device buzzard_labels (9):#453 -> buzzard_labels (9):A161
- U$56: device buzzard_labels (14):182 -> buzzard_labels (11):EDGE_20
- U$57: device buzzard_labels (14):193 -> buzzard_labels (13):171
- U$58: device buzzard_labels (11):EDGE_20 -> buzzard_labels (14):182
- U$59: device buzzard_labels:GND0 -> buzzard_labels (14):193
- U$61: device buzzard_labels:VDD1 -> buzzard_labels (1):MEAS10
- U$64: device buzzard_labels:BLK2 -> buzzard_labels:VDD1
- U$65: device buzzard_labels:GRN1 -> buzzard_labels:VDD1
- U$66: device buzzard_labels:372 -> buzzard_labels:GND0
- U$67: device Labels:QWIIC_COPYRIGHT_SMALL -> buzzard_labels:RST15
- U$68: device buzzard_labels:CAMERA3 -> buzzard_labels:BLK2
- U$70: device buzzard_labels:MIC00 -> buzzard_labels:372
- U$72: device SparkFun-Aesthetics:SFE_LOGO_NAME_.1 -> buzzard_labels:CAMERA3
- U$78: device buzzard_labels (9):MIC10 -> buzzard_labels (9):#444
- U$82: device buzzard_labels (9):#444 -> buzzard_labels (9):MIC10
- U$88: device buzzard_labels:GND0 -> buzzard_labels (13):171
- U$89: device buzzard_labels:VDD1 -> buzzard_labels (14):182
- U$90: device buzzard_labels:VDD1 -> buzzard_labels (14):193
- U$92: device buzzard_labels:RST15 -> buzzard_labels (1):MEAS10
- U$93: device buzzard_labels:BLK2 -> buzzard_labels (1):MEAS10
- U$94: device buzzard_labels:GRN1 -> buzzard_labels:GND0
- U$95: device buzzard_labels:372 -> buzzard_labels:VDD1
- U$96: device Labels:QWIIC_COPYRIGHT_SMALL -> buzzard_labels:VDD1
- U$97: device buzzard_labels:CAMERA3 -> buzzard_labels:GND0
- U$99: device buzzard_labels:MIC00 -> buzzard_labels:BLK2
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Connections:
- new net VDD_ACCEL: C20.1, C21.1, R25.1, R26.1, U2.10, U2.2, U2.3, U2.9, U5.D41
- new net VDD_ACCEL1: C12.1, C8.1, R12.1, R13.1, U1.10, U1.2, U1.3, U1.9, U6.D41
- new net VDD_ACCEL2: C31.1, C32.1, R22.1, R23.1, U7.10, U7.2, U7.3, U7.9, U9.D41
- new net VDD_ACCEL3: C45.1, C46.1, R36.1, R37.1, U10.10, U10.2, U10.3, U10.9, U12.D41
- new net VDD_ACCEL4: C59.1, C60.1, R46.1, R47.1, U13.10, U13.2, U13.3, U13.9, U15.D41
- new net VDD_ACCEL5: C73.1, C74.1, R56.1, R57.1, U16.10, U16.2, U16.3, U16.9, U18.D41
- new net VDD_ACCEL6: C87.1, C88.1, R66.1, R67.1, U19.10, U19.2, U19.3, U19.9, U21.D41
- new net VDD_ACCEL7: C101.1, C102.1, R76.1, R77.1, U22.10, U22.2, U22.3, U22.9, U24.D41
- new net VDD_ACCEL8: C115.1, C116.1, R86.1, R87.1, U25.10, U25.2, U25.3, U25.9, U27.D41
- new net VDD_PDM: C1.1, C18.1, E1.5, E2.2, E2.5, U5.D0
- new net VDD_PDM1: C24.1, C28.1, E3.5, E4.2, E4.5, U6.D0
- new net VDD_PDM2: C38.1, C42.1, E5.5, E6.2, E6.5, U9.D0
- new net VDD_PDM3: C52.1, C56.1, E7.5, E8.2, E8.5, U12.D0
- new net VDD_PDM4: C66.1, C70.1, E10.2, E10.5, E9.5, U15.D0
- new net VDD_PDM5: C80.1, C84.1, E11.5, E12.2, E12.5, U18.D0
- new net VDD_PDM6: C94.1, C98.1, E13.5, E14.2, E14.5, U21.D0
- new net VDD_PDM7: C108.1, C112.1, E15.5, E16.2, E16.5, U24.D0
- new net VDD_PDM8: C122.1, C126.1, E17.5, E18.2, E18.5, U27.D0
- new net VIN1: D1.C, D2.C, JP1.1, JP1.3
- new net VIN2: D7.C, D8.C, JP2.1, JP2.3
- new net VIN3: D13.C, D14.C, JP3.1, JP3.3
- new net VIN4: D19.C, D20.C, JP4.1, JP4.3
- new net VIN5: D25.C, D26.C, JP5.1, JP5.3
- new net VIN6: D31.C, D32.C, JP6.1, JP6.3
- new net VIN7: D37.C, D38.C, JP7.1, JP7.3
- new net VIN8: D43.C, D44.C, JP8.1, JP8.3
- new net VIN9: D49.C, D50.C, JP9.1, JP9.3
- net !DTR: now also R1.2; no longer R29.2
- net !DTR1: now also R16.2; no longer R23.2
- net !DTR2: now also R30.2; no longer R42.2
- net !DTR3: now also R40.2; no longer R56.2
- net !DTR4: now also R50.2; no longer R70.2
- net !DTR5: now also R60.2; no longer R84.2
- net !DTR6: now also R70.2; no longer R98.2
- net !DTR7: now also R80.2; no longer R112.2
- net !DTR8: now also R90.2; no longer R126.2
- net ACCEL_I2C_SCL: no longer R12.1
- net ACCEL_I2C_SCL1: no longer R3.1
- net ACCEL_I2C_SCL2: no longer R31.1
- net ACCEL_I2C_SCL3: no longer R45.1
- net ACCEL_I2C_SCL4: no longer R59.1
- net ACCEL_I2C_SCL5: no longer R73.1
- net ACCEL_I2C_SCL6: no longer R87.1
- net ACCEL_I2C_SCL7: no longer R101.1
- net ACCEL_I2C_SCL8: no longer R115.1
- net ACCEL_I2C_SDA: no longer R14.1
- net ACCEL_I2C_SDA1: no longer R4.1
- net ACCEL_I2C_SDA2: no longer R32.1
- net ACCEL_I2C_SDA3: no longer R46.1
- net ACCEL_I2C_SDA4: no longer R60.1
- net ACCEL_I2C_SDA5: no longer R74.1
- net ACCEL_I2C_SDA6: no longer R88.1
- net ACCEL_I2C_SDA7: no longer R102.1
- net ACCEL_I2C_SDA8: no longer R116.1
- net ACCEL_INT1: now also U5.D2
- net ACCEL_INT10: now also R46.2, U15.D1; no longer R66.2
- net ACCEL_INT11: now also R57.2, U18.D2; no longer R81.2
- net ACCEL_INT12: now also R56.2, U18.D1; no longer R80.2
- net ACCEL_INT13: now also R67.2, U21.D2; no longer R95.2
- net ACCEL_INT14: now also R66.2, U21.D1; no longer R94.2
- net ACCEL_INT15: now also R77.2, U24.D2; no longer R109.2
- net ACCEL_INT16: now also R76.2, U24.D1; no longer R108.2
- net ACCEL_INT17: now also R87.2, U27.D2; no longer R123.2
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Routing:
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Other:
- board text added: "v22"
- board text removed: "v21"
